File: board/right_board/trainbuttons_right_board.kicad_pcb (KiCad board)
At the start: 4 copper layers, 87 x 95 mm, 13 parts, among them J301 HDMI_A, SW301 SW_Push, SW302 SW_Push, SW303 SW_Push, SW304 SW_Push, SW305 SW_Push, SW306 SW_Push, SW307 SW_Push, SW308 SW_Push

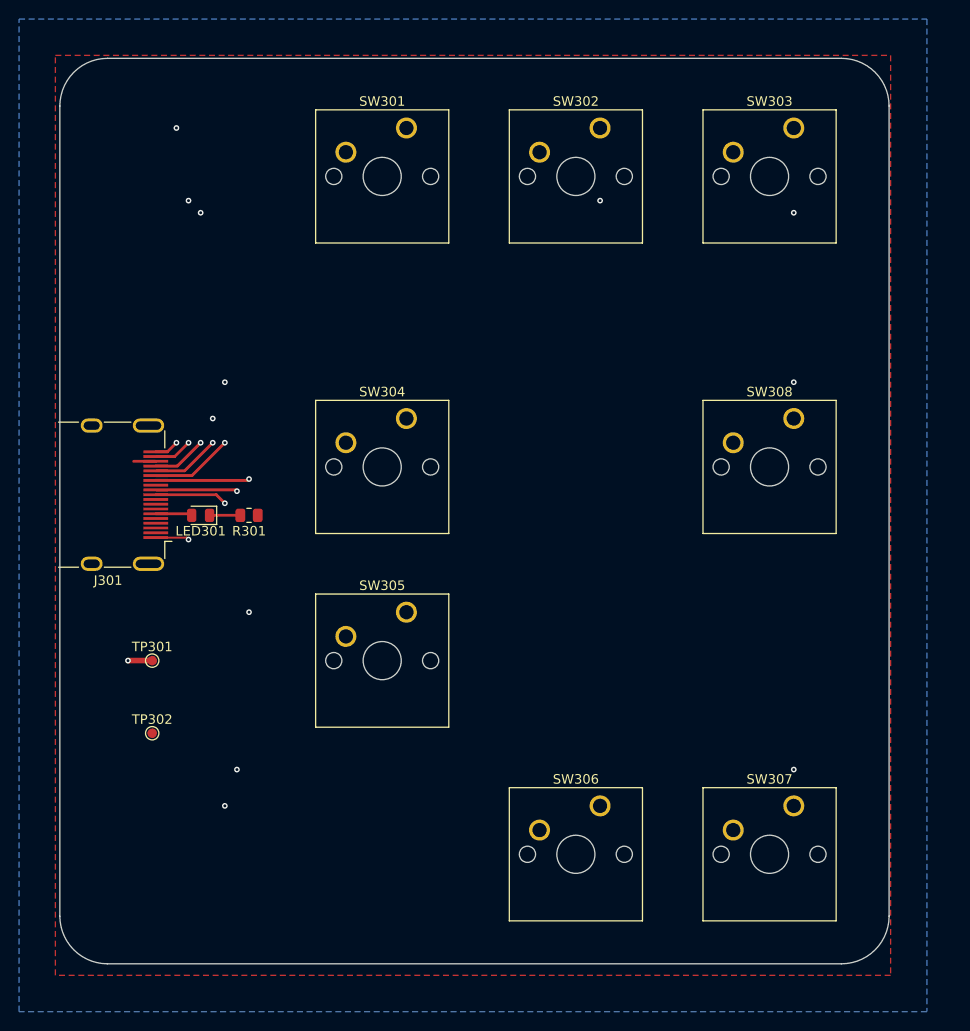
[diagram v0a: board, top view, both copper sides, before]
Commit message: boards: add JLCPCB mounting holes
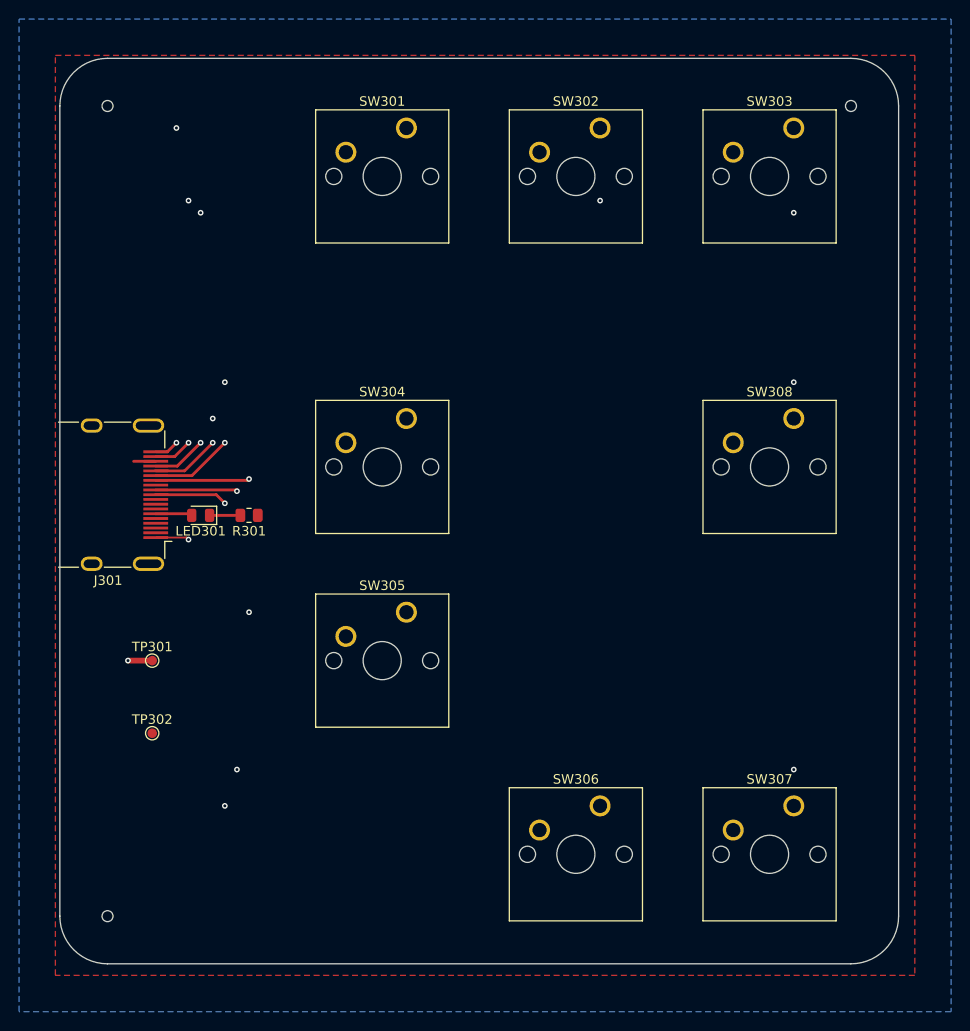
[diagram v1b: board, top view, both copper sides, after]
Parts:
- added REF**: JLCPCB_Mounting_Hole, JLCPCB:JLCPCB_Mounting_Hole, F.Cu at (250.6, 33.2)
- added REF**: JLCPCB_Mounting_Hole, JLCPCB:JLCPCB_Mounting_Hole, F.Cu at (250.6, 118.2)
- added REF**: JLCPCB_Mounting_Hole, JLCPCB:JLCPCB_Mounting_Hole, F.Cu at (328.6, 33.2)
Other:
- board size 87 x 95 mm -> 88 x 95 mm
